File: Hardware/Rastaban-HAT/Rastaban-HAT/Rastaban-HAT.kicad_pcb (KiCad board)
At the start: 4 copper layers, 68.7 x 65.4 mm, 86 parts, among them IC2 BCM53DS, J1 1778780, J10 GPIO, J11 Conn_01x06_Male, J2 1778780, J3 1778780, J4 Screw_Terminal_01x02, J5 Jack-DC 12V+, J6 SM04B-SRSS-TB(LF)(SN), J7 Screw_Terminal_01x02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

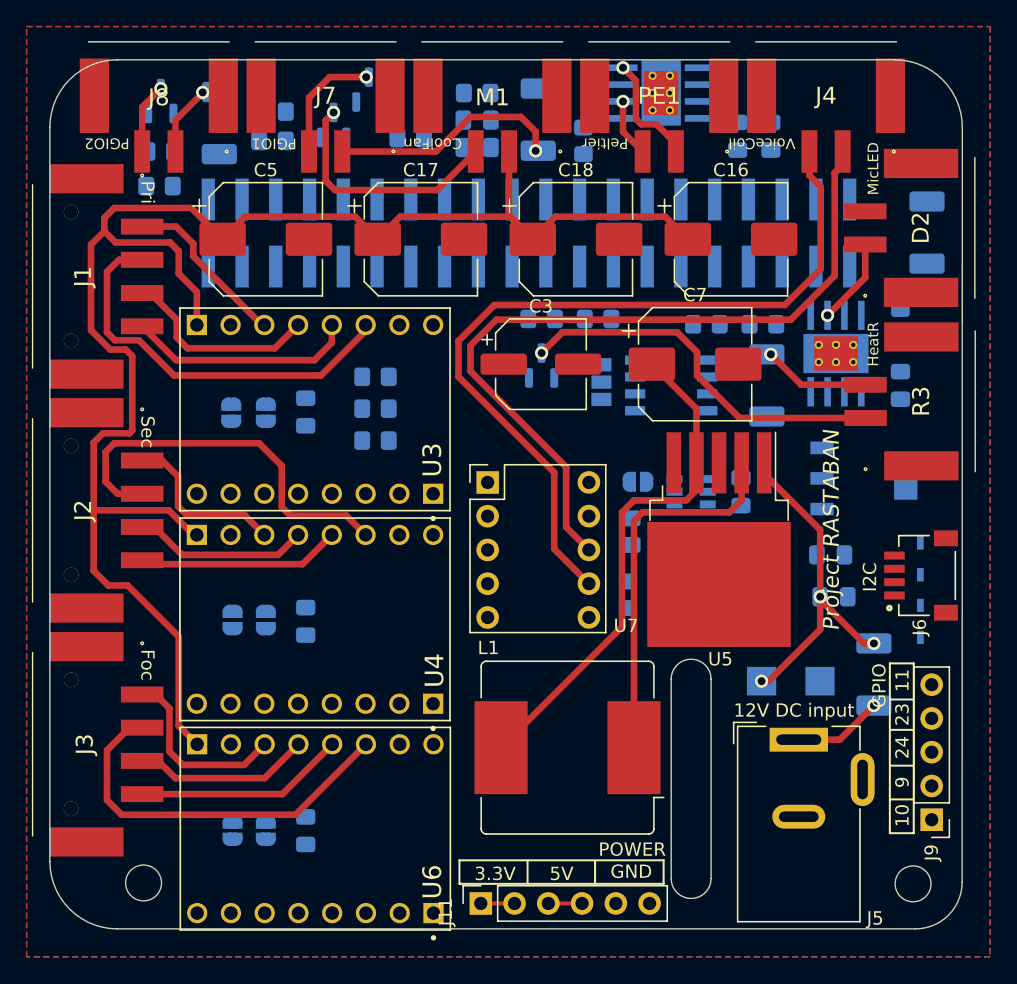
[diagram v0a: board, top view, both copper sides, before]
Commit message: routing 4 layers
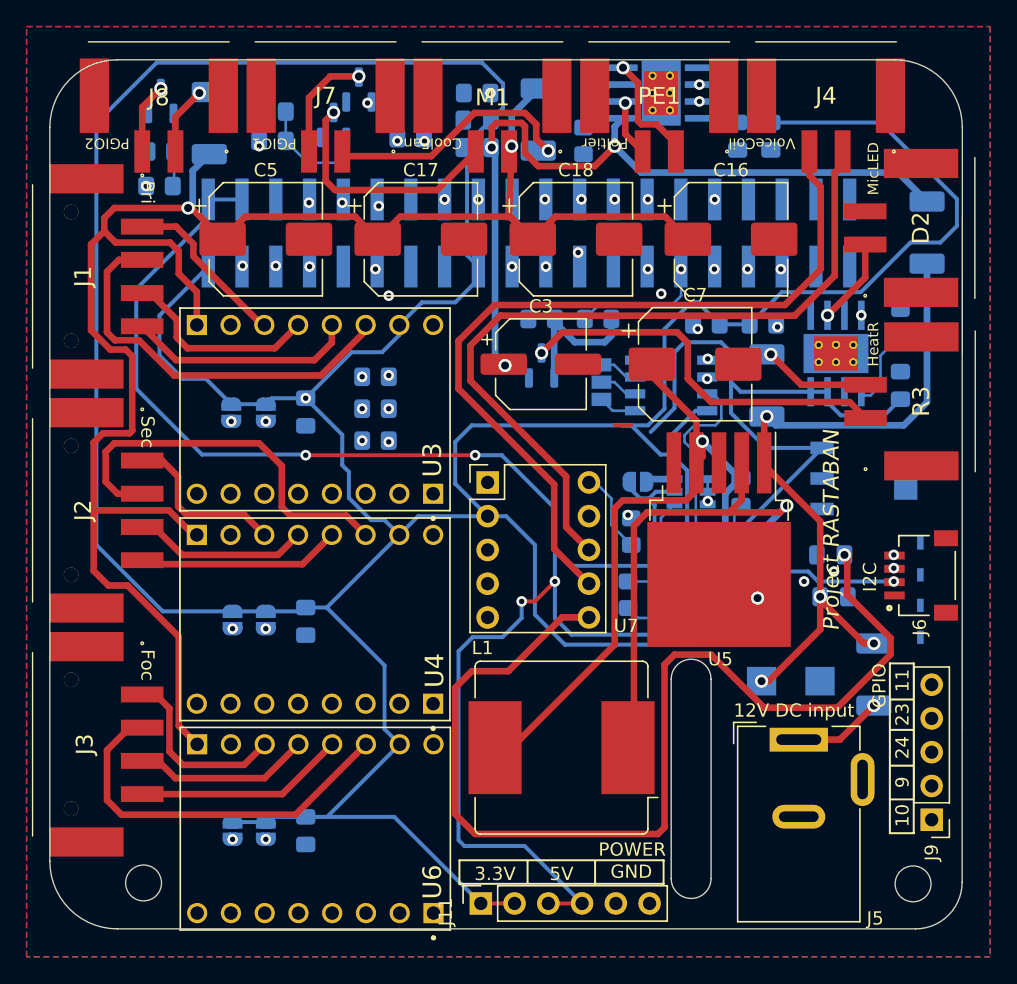
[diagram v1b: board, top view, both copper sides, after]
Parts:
- moved F3 0.75 mm to (106.2, 72.3)
- moved Q2 0.75 mm to (117.5, 69.7)
- moved L1 0.45 mm to (132.8, 119.3)
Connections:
- J10 pad 36: STEPFOCUS -> unconnected-(J10-Pad36)
- J10 pad 38: DIRFOCUS -> unconnected-(J10-Pad38)
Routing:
- net 3.3V+: track 2.54 -> 350.4 mm, vias 0 -> 2
- net 5V+: track 2.54 -> 188.8 mm, vias 0 -> 4
- net Net-(C15-Pad2): track 0.00 -> 80.1 mm, vias 0 -> 1
- net RX: track 0.00 -> 68.9 mm, vias 0 -> 4
- net SDA: track 0.00 -> 65.4 mm, vias 0 -> 3
- net GPIO23: track 0.00 -> 59.9 mm, vias 0 -> 1
- net GPIO24: track 0.00 -> 58.5 mm, vias 0 -> 1
- net Net-(C2-Pad2): track 0.00 -> 58.4 mm, vias 0 -> 3
- net GPIO10: track 0.00 -> 57.8 mm, vias 0 -> 1
- net SCL: track 0.00 -> 57.4 mm, vias 0 -> 3
- net GPIO9: track 0.00 -> 53.3 mm, vias 0 -> 1
- net GPIO11: track 0.00 -> 45.9 mm, vias 0 -> 1
- net CTRLLED: track 0.00 -> 44.7 mm, vias 0 -> 2
- net CTRLFAN: track 0.00 -> 43.1 mm, vias 0 -> 3
- net 12V+: track 151.9 -> 189.3 mm, vias 3 -> 6
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- added copper zone on B.Cu, net GND
- added copper zone on F.Cu, net GND
- removed copper zone on B.Cu, net 12V+
- removed copper zone on F.Cu, net 12V+

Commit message: 4 layer PCB finished
ERC
Error: 0
Warnings: 18
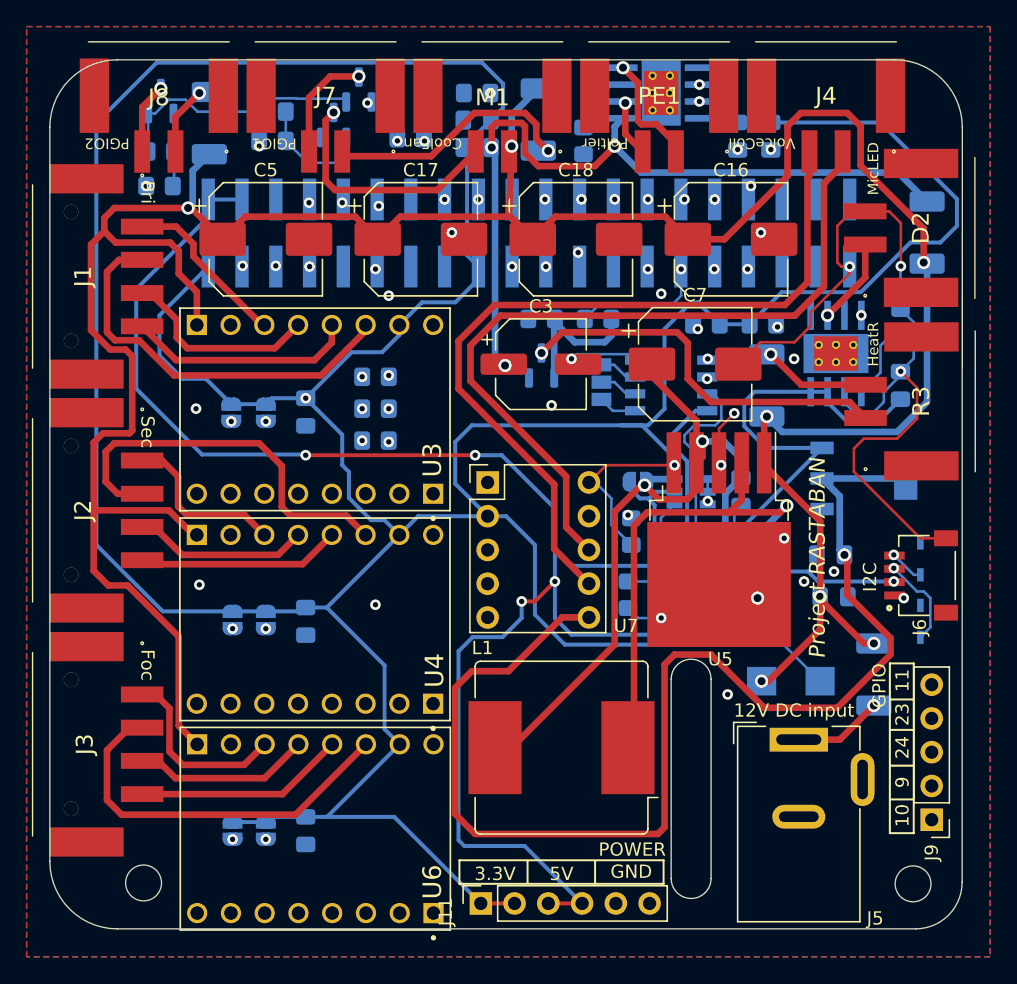
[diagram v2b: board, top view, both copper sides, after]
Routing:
- net GND: track 21.3 -> 126.9 mm, vias 1 -> 23
- net 12V+: track 189.3 -> 221.7 mm, vias 6 -> 7
- net 5V+: track 188.8 -> 172.6 mm
- net Net-(C15-Pad2): track 80.1 -> 92.9 mm
- net ID_SDA: track 6.24 -> 15.0 mm
- net SCL: track 57.4 -> 65.1 mm
- net SDA: track 65.4 -> 67.3 mm
- net Net-(C13-Pad2): track 57.0 -> 58.6 mm, vias 1 -> 2
- net 3.3V+: track 350.4 -> 349.6 mm
- net /FocusMotors/out1: track 61.0 -> 60.3 mm
- net unconnected-(J10-Pad36): vias 1 -> 0

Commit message: Warnings reduced to 10.
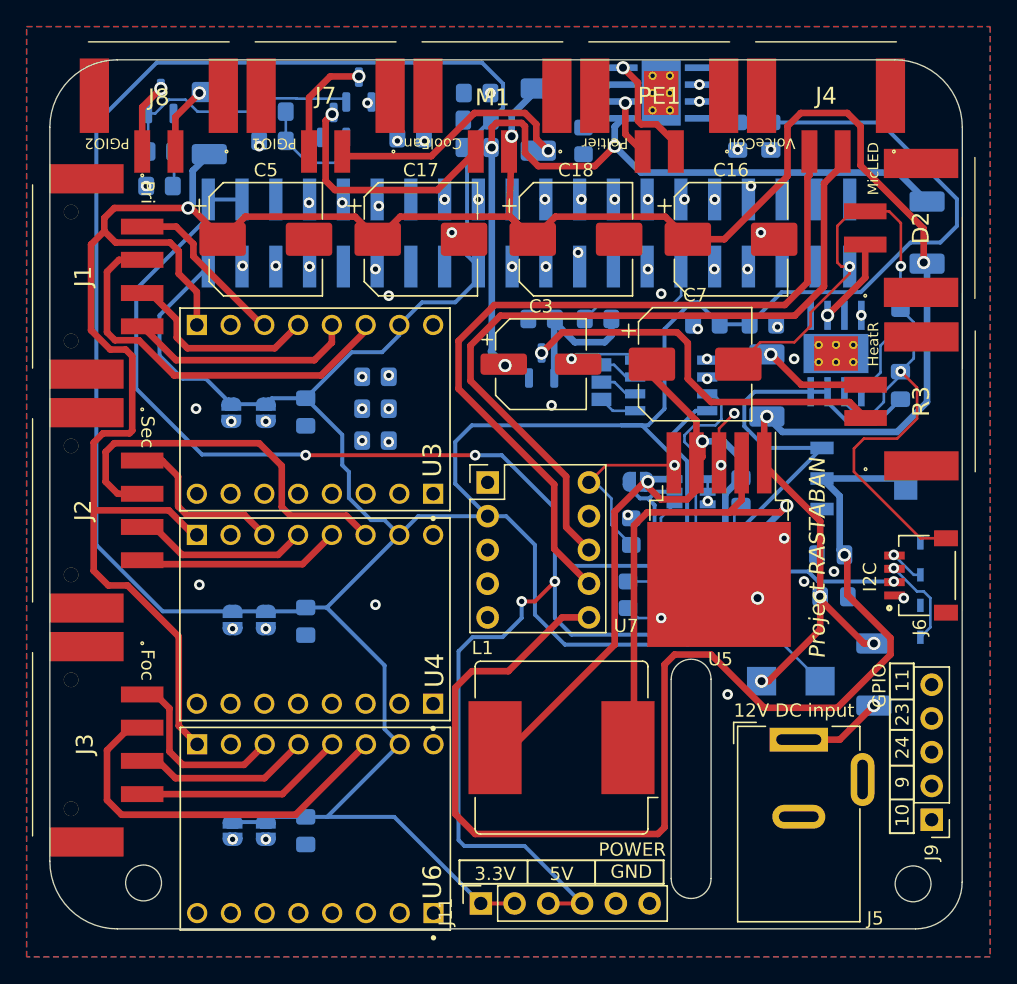
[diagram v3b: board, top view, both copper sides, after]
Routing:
- net 12V+: track 221.7 -> 221.0 mm
- net CTRLHEAT: vias 1 -> 0
- net 3.3V+: vias 2 -> 1
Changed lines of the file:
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@@
   )
   (segment (start 129.215 130.975) (end 126.675 130.975) (width 0.3) (layer "F.Cu") (net 1))
-  (via (at 113.5 92.9625) (size 0.8) (drill 0.4) (layers "F.Cu" "B.Cu") (net 1))
   (via (at 157.75 106.75) (size 0.8) (drill 0.4) (layers "F.Cu" "B.Cu") (net 1))
   (segment (start 110.5 93.408) (end 107.9 93.408) (width 0.3) (layer "B.Cu") (net 1))
@@
   (segment (start 128.8 79.2167) (end 130.5833 81) (width 0.5) (layer "F.Cu") (net 3))
   (segment (start 97.55 105.95) (end 97.55 101.4) (width 0.5) (layer "F.Cu") (net 3))
-  (via (at 129 74) (size 1) (drill 0.6) (layers "F.Cu" "B.Cu") (net 3))
+  (via (at 129 73.25) (size 1) (drill 0.6) (layers "F.Cu" "B.Cu") (net 3))
   (via (at 148.2 94.3375) (size 1) (drill 0.6) (layers "F.Cu" "B.Cu") (net 3))
   (via (at 160 82.75) (size 1) (drill 0.6) (layers "F.Cu" "B.Cu") (net 3))
@@
   (segment (start 158 95.5) (end 149.3625 95.5) (width 0.5) (layer "B.Cu") (net 3))
   (segment (start 149.3625 95.5) (end 148.2 94.3375) (width 0.5) (layer "B.Cu") (net 3))
-  (segment (start 129 74) (end 129 71.6625) (width 0.5) (layer "B.Cu") (net 3))
   (segment (start 160.0875 82.8375) (end 160 82.75) (width 0.5) (layer "B.Cu") (net 3))
   (segment (start 106.25 74.6) (end 105 75.85) (width 0.5) (layer "B.Cu") (net 3))
+  (segment (start 105 75.85) (end 105 78.3) (width 0.5) (layer "B.Cu") (net 3))
   (segment (start 129 71.6625) (end 131 69.6625) (width 0.5) (layer "B.Cu") (net 3))
-  (segment (start 105 75.85) (end 105 78.3) (width 0.5) (layer "B.Cu") (net 3))
   (segment (start 105 78.3) (end 104.65 78.65) (width 0.5) (layer "B.Cu") (net 3))
   (segment (start 160.25 82.8375) (end 160.0875 82.8375) (width 0.5) (layer "B.Cu") (net 3))
-  (segment (start 140.075 100.575) (end 142.2 100.575) (width 0.5) (layer "F.Cu") (net 4))
-  (segment (start 128.2 119.253) (end 128.997 119.253) (width 0.5) (layer "F.Cu") (net 4))
+  (segment (start 129 73.25) (end 129 71.6625) (width 0.5) (layer "B.Cu") (net 3))
+  (segment (start 142.9 99.875) (end 142.9 97.825) (width 0.5) (layer "F.Cu") (net 4))
   (segment (start 139.55 91.3) (end 142.9 94.65) (width 0.5) (layer "F.Cu") (net 4))
-  (segment (start 138.75 99.5) (end 139 99.5) (width 0.5) (layer "F.Cu") (net 4))
+  (segment (start 136.75 101.5) (end 136.75 111.5) (width 0.5) (layer "F.Cu") (net 4))
+  (segment (start 142.2 100.575) (end 142.9 99.875) (width 0.5) (layer "F.Cu") (net 4))
+  (segment (start 139.25 99.625) (end 140.2 100.575) (width 0.5) (layer "F.Cu") (net 4))
   (segment (start 143.350498 96.2005) (end 143.350498 97.374502) (width 0.5) (layer "F.Cu") (net 4))
-  (segment (start 142.2 100.575) (end 142.9 99.875) (width 0.5) (layer "F.Cu") (net 4))
   (segment (start 143.350498 97.374502) (end 142.9 97.825) (width 0.5) (layer "F.Cu") (net 4))
+  (segment (start 128.997 119.253) (end 128.2 119.253) (width 0.5) (layer "F.Cu") (net 4))
   (segment (start 139.55 90.4) (end 139.55 91.3) (width 0.5) (layer "F.Cu") (net 4))
-  (segment (start 128.997 119.253) (end 136.75 111.5) (width 0.5) (layer "F.Cu") (net 4))
+  (segment (start 139.25 99.25) (end 139 99.25) (width 0.5) (layer "F.Cu") (net 4))
+  (segment (start 139.25 99.25) (end 139.25 99.625) (width 0.5) (layer "F.Cu") (net 4))
+  (segment (start 136.75 111.5) (end 128.997 119.253) (width 0.5) (layer "F.Cu") (net 4))
   (segment (start 142.9 94.65) (end 142.9 97.825) (width 0.5) (layer "F.Cu") (net 4))
-  (segment (start 139 99.5) (end 140.075 100.575) (width 0.5) (layer "F.Cu") (net 4))
-  (segment (start 136.75 101.5) (end 138.75 99.5) (width 0.5) (layer "F.Cu") (net 4))
-  (segment (start 136.75 111.5) (end 136.75 101.5) (width 0.5) (layer "F.Cu") (net 4))
-  (segment (start 142.9 99.875) (end 142.9 97.825) (width 0.5) (layer "F.Cu") (net 4))
+  (segment (start 139 99.25) (end 136.75 101.5) (width 0.5) (layer "F.Cu") (net 4))
+  (segment (start 140.2 100.575) (end 142.2 100.575) (width 0.5) (layer "F.Cu") (net 4))
   (via (at 143.350498 96.2005) (size 1) (drill 0.6) (layers "F.Cu" "B.Cu") (net 4))
-  (via (at 139 99.5) (size 1) (drill 0.6) (layers "F.Cu" "B.Cu") (net 4))
+  (via (at 139.25 99.25) (size 1) (drill 0.6) (layers "F.Cu" "B.Cu") (net 4))
   (segment (start 143.1375 106.1125) (end 145.075 104.175) (width 0.5) (layer "B.Cu") (net 4))
   (segment (start 144.9505 96.2005) (end 143.350498 96.2005) (width 0.5) (layer "B.Cu") (net 4))
@@
   (segment (start 99.1 96.35) (end 98.45 97) (width 0.5) (layer "F.Cu") (net 18))
   (segment (start 118.007 103.2465) (end 116.5605 101.8) (width 0.5) (layer "F.Cu") (net 18))
-  (segment (start 101.2 100.15) (end 101.15 100.2) (width 0.5) (layer "F.Cu") (net 18))
   (segment (start 99.35 100.15) (end 101.2 100.15) (width 0.5) (layer "F.Cu") (net 18))
   (segment (start 98.45 97) (end 98.45 99.25) (width 0.5) (layer "F.Cu") (net 18))
@@
   (via (at 143 87.75) (size 0.8) (drill 0.4) (layers "F.Cu" "B.Cu") (net 42))
   (via (at 143.707059 91.505368) (size 0.8) (drill 0.4) (layers "F.Cu" "B.Cu") (net 42))
-  (segment (start 142.9995 87.75) (end 143 87.75) (width 0.2) (layer "In1.Cu") (net 42))
   (segment (start 142.65 87.4) (end 142.65 81.4) (width 0.2) (layer "In1.Cu") (net 42))
   (segment (start 143 87.75) (end 142.65 87.4) (width 0.2) (layer "In1.Cu") (net 42))
@@
   (segment (start 143 90.798309) (end 143.707059 91.505368) (width 0.2) (layer "In2.Cu") (net 42))
   (segment (start 143 87.75) (end 143 90.798309) (width 0.2) (layer "In2.Cu") (net 42))
-  (via (at 143.75 90) (size 0.8) (drill 0.4) (layers "F.Cu" "B.Cu") (net 43))
+  (via (at 143.6995 90) (size 0.8) (drill 0.4) (layers "F.Cu" "B.Cu") (net 43))
   (via (at 139.25 83.25) (size 0.8) (drill 0.4) (layers "F.Cu" "B.Cu") (net 43))
   (via (at 149 87.5995) (size 0.8) (drill 0.4) (layers "F.Cu" "B.Cu") (net 43))
-  (segment (start 147.8495 88.75) (end 145 88.75) (width 0.2) (layer "In1.Cu") (net 43))
-  (segment (start 145 88.75) (end 143.75 90) (width 0.2) (layer "In1.Cu") (net 43))
+  (segment (start 143.6995 89.9495) (end 141.25 87.5) (width 0.2) (layer "In1.Cu") (net 43))
   (segment (start 141.25 87.5) (end 141.25 85) (width 0.2) (layer "In1.Cu") (net 43))
+  (segment (start 144.9495 88.75) (end 147.8495 88.75) (width 0.2) (layer "In1.Cu") (net 43))
+  (segment (start 143.6995 90) (end 143.6995 89.9495) (width 0.2) (layer "In1.Cu") (net 43))
+  (segment (start 147.8495 88.75) (end 149 87.5995) (width 0.2) (layer "In1.Cu") (net 43))
+  (segment (start 143.6995 90) (end 144.9495 88.75) (width 0.2) (layer "In1.Cu") (net 43))
+  (segment (start 141.25 85) (end 139.5 83.25) (width 0.2) (layer "In1.Cu") (net 43))
   (segment (start 139.5 83.25) (end 139.25 83.25) (width 0.2) (layer "In1.Cu") (net 43))
-  (segment (start 141.25 85) (end 139.5 83.25) (width 0.2) (layer "In1.Cu") (net 43))
-  (segment (start 143.75 90) (end 141.25 87.5) (width 0.2) (layer "In1.Cu") (net 43))
-  (segment (start 149 87.5995) (end 147.8495 88.75) (width 0.2) (layer "In1.Cu") (net 43))
-  (via (at 141.75 83.25) (size 0.8) (drill 0.4) (layers "F.Cu" "B.Cu") (net 44))
   (segment (start 135.5 86) (end 134.5 87) (width 0.2) (layer "B.Cu") (net 44))
   (segment (start 141.75 85.25) (end 141 86) (width 0.2) (layer "B.Cu") (net 44))
@@
   (segment (start 136.75 74) (end 136.75 72.53) (width 0.5) (layer "B.Cu") (net 70))
   (segment (start 138.733 75.983) (end 136.75 74) (width 0.5) (layer "B.Cu") (net 70))
-  (segment (start 127.75 89.75) (end 127.75 74.5) (width 0.5) (layer "B.Cu") (net 70))
-  (segment (start 127.75 74.5) (end 127.5 74.25) (width 0.5) (layer "B.Cu") (net 70))
+  (segment (start 127.5 89.375) (end 127.5 74.25) (width 0.5) (layer "B.Cu") (net 70))
   (segment (start 160.25 78.1625) (end 158.0705 75.983) (width 0.5) (layer "B.Cu") (net 70))
+  (segment (start 127.4375 89.4375) (end 127.5 89.375) (width 0.5) (layer "B.Cu") (net 70))
   (segment (start 136.75 72.53) (end 137.375 71.905) (width 0.5) (layer "B.Cu") (net 70))
-  (segment (start 128.5 90.5) (end 127.75 89.75) (width 0.5) (layer "B.Cu") (net 70))
+  (segment (start 128.5 90.5) (end 127.4375 89.4375) (width 0.5) (layer "B.Cu") (net 70))
   (segment (start 158.0705 75.983) (end 138.733 75.983) (width 0.5) (layer "B.Cu") (net 70))
   (via (at 107.9 94.708) (size 0.8) (drill 0.4) (layers "F.Cu" "B.Cu") (net 71))
@@
   (segment (start 157 92.5) (end 158.25 91.25) (width 0.2) (layer "B.Cu") (net 96))
   (segment (start 104.459682 70.5) (end 105.359682 71.4) (width 0.2) (layer "B.Cu") (net 96))
-  (segment (start 115 72.0625) (end 115.6 71.4625) (width 0.5) (layer "F.Cu") (net 97))
-  (segment (start 115.7 77.3) (end 115 76.6) (width 0.5) (layer "F.Cu") (net 97))
-  (segment (start 123.4 77.3) (end 115.7 77.3) (width 0.5) (layer "F.Cu") (net 97))
-  (segment (start 126.3 74.4) (end 123.4 77.3) (width 0.5) (layer "F.Cu") (net 97))
-  (segment (start 115 76.6) (end 115 72.0625) (width 0.5) (layer "F.Cu") (net 97))
-  (via (at 115.6 71.4625) (size 1) (drill 0.6) (layers "F.Cu" "B.Cu") (net 97))
+  (segment (start 115.7 77.3) (end 123.4 77.3) (width 0.5) (layer "F.Cu") (net 97))
+  (segment (start 123.4 77.3) (end 126.3 74.4) (width 0.5) (layer "F.Cu") (net 97))
+  (segment (start 115 76.6) (end 115.7 77.3) (width 0.5) (layer "F.Cu") (net 97))
+  (segment (start 115 72.082075) (end 115 76.6) (width 0.5) (layer "F.Cu") (net 97))
+  (segment (start 115.490823 71.591252) (end 115 72.082075) (width 0.5) (layer "F.Cu") (net 97))
+  (via (at 115.490823 71.591252) (size 1) (drill 0.6) (layers "F.Cu" "B.Cu") (net 97))
   (zone (net 96) (net_name "GND") (layers F&B.Cu) (hatch edge 0.508)
     (connect_pads (clearance 0.508))

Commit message: V0.3 4 layer rounded traces design finished
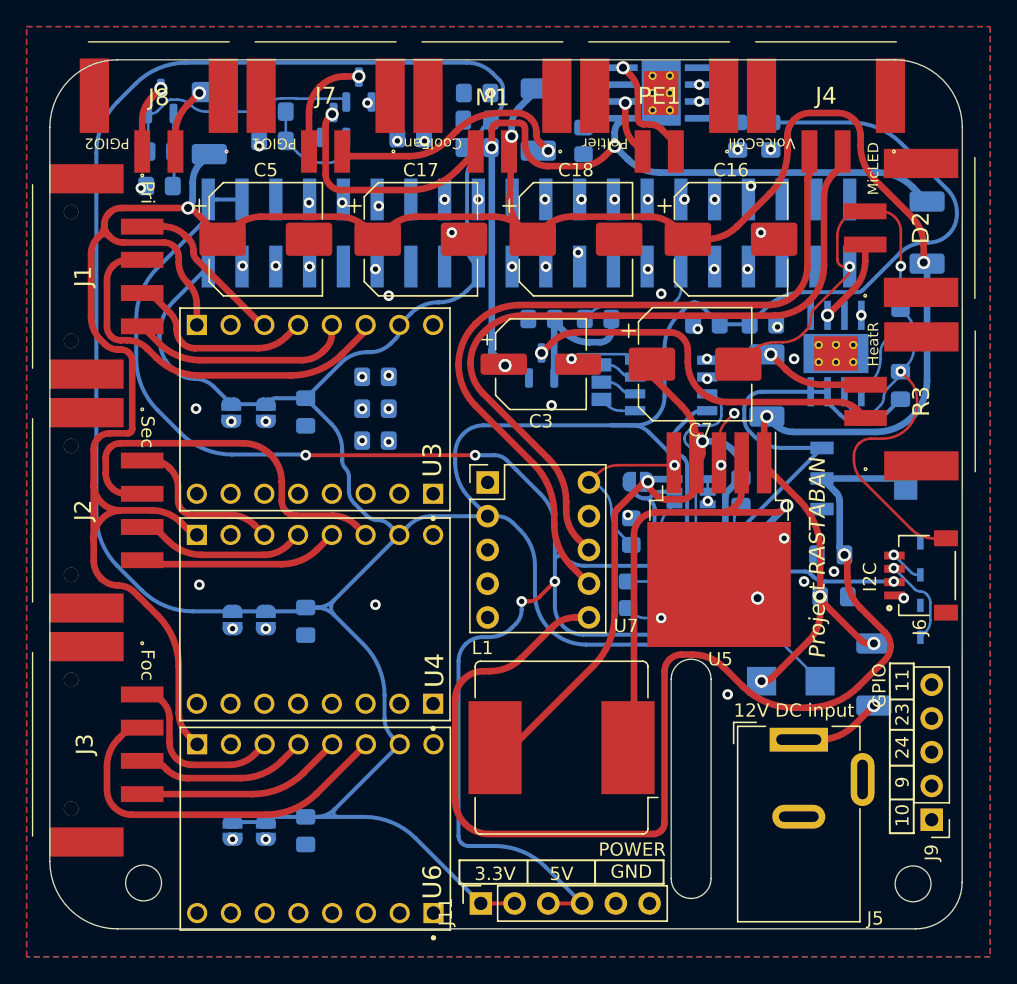
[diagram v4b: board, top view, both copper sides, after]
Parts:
- renumbered F1 to 11
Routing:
- net GND: track 126.9 -> 123.7 mm
- net 5V+: track 172.6 -> 169.7 mm
- net Net-(C15-Pad2): track 92.9 -> 90.9 mm
- net GPIO23: track 59.9 -> 58.5 mm
- net /FocusMotors/out1: track 60.3 -> 58.9 mm
- net SDA: track 67.3 -> 65.9 mm
- net /FocusMotors/out2: track 58.2 -> 56.8 mm
- net GPIO10: track 57.8 -> 56.4 mm
- net SCL: track 65.1 -> 63.9 mm
- net CTRLLED: track 44.7 -> 43.4 mm
- net 3.3V+: track 349.6 -> 348.3 mm
- net GPIO24: track 58.5 -> 57.3 mm
- net GPIO9: track 53.3 -> 52.1 mm
- net CTRLFAN: track 43.1 -> 42.2 mm
- net RX: track 68.9 -> 68.0 mm
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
